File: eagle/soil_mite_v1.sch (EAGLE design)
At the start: 31 parts, among them U4 TEMP_SENSOR_LMT84, U5 TRISTATE_BUFFER_SOT353, X1 1365-10

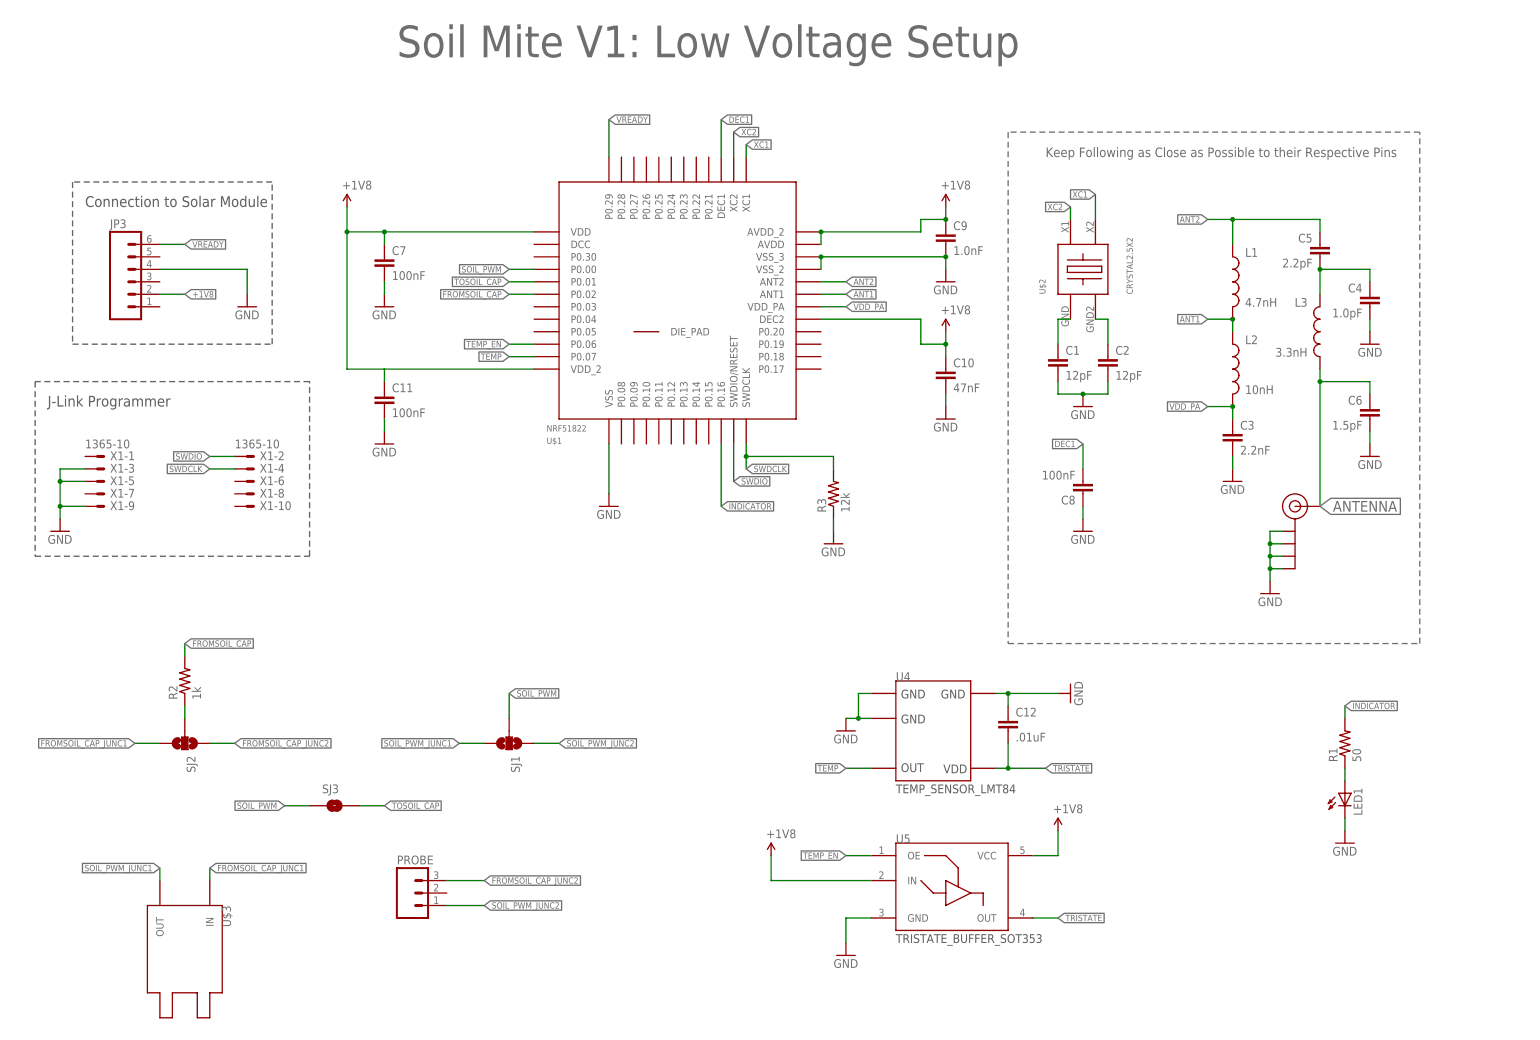
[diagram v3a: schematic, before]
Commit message: finalized soil mite design. sending out for shipping
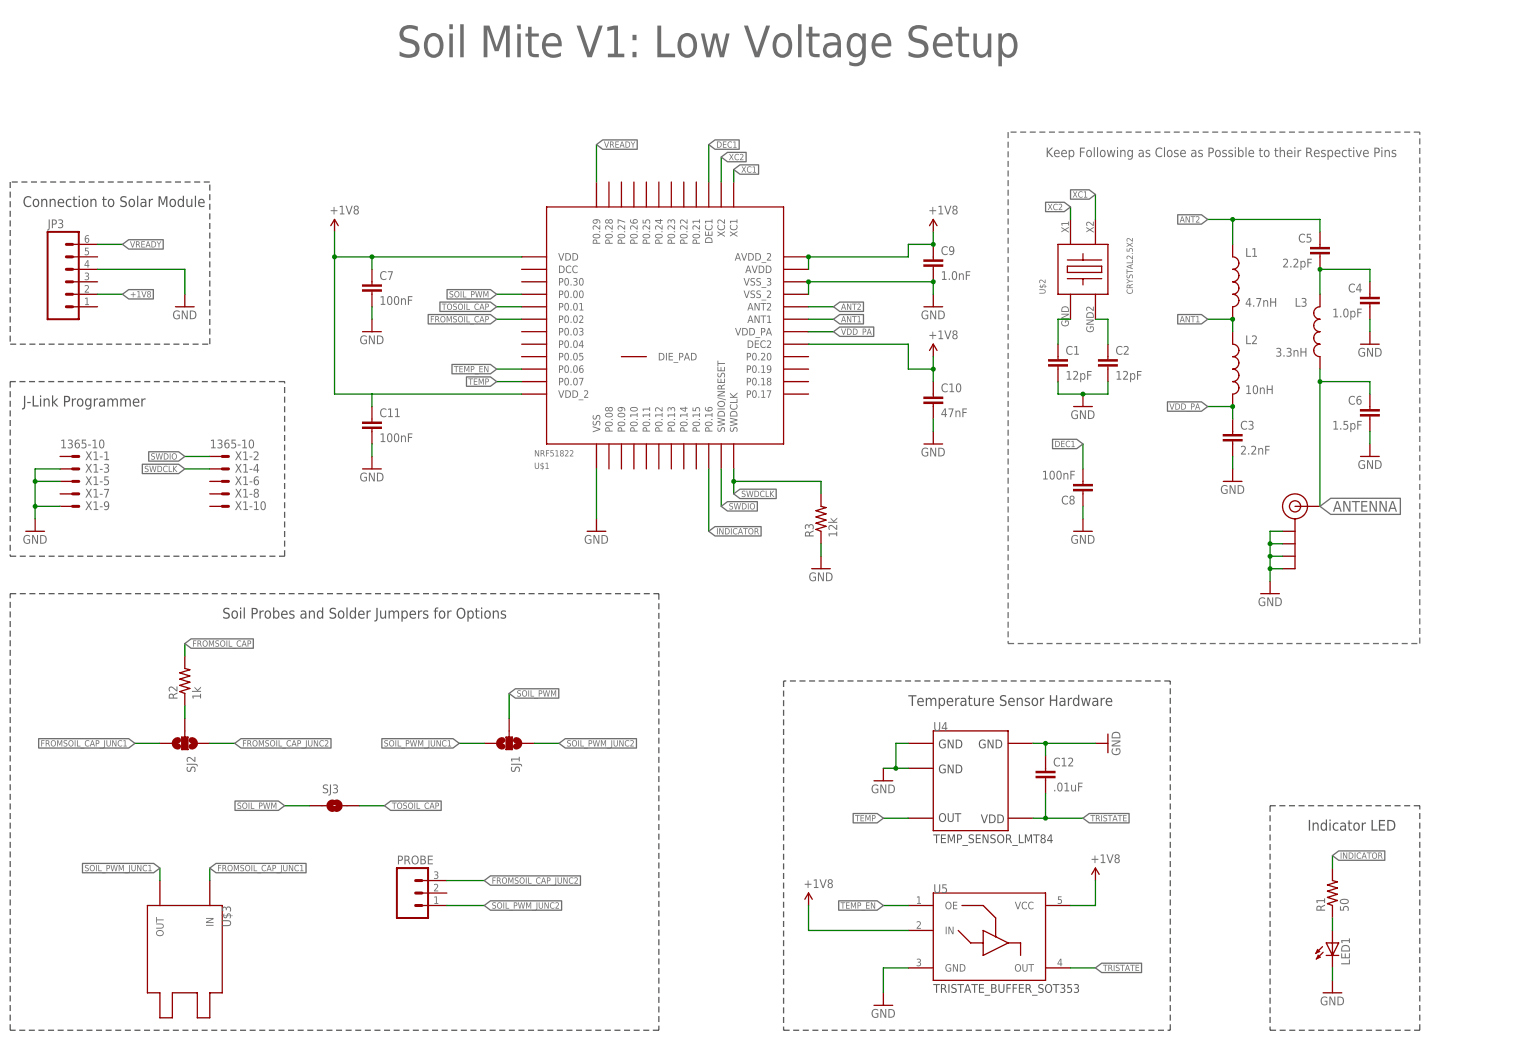
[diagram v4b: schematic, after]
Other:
- note added: "Indicator LED"
- note added: "Soil Probes and Solder Jumpers for Options"
- note added: "Temperature Sensor Hardware"
- moved on the sheet: C10, C11, C12, C7, C9, JP3, LED1, R1, R3, U$1, U4, U5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
